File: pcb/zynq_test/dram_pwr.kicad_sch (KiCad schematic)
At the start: 47 parts, among them U401 MT41K256M16TW-107, U402 MT41K256M16TW-107, U501 LP2998

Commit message: Finished Power Supply
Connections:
- net +3.3V renamed +3V3
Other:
- title: (none) -> DDR3 Power
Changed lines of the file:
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@@
 	(paper "A4")
 	(title_block
-		(date "2025-09-06")
-		(rev "v1.0")
+		(title "DDR3 Power")
+		(date "2025-09-13")
+		(rev "A")
 	)
 	(rectangle
@@
 			)
 		)
-		(property "Value" "+3.3V"
+		(property "Value" "+3V3"
 			(at 203.2 80.01 0)
 			(effects

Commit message: Finished to first ddr ic
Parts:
- U401, U402: footprint dram:BGA96C80P9X16_1400X800X120 -> dram:BGA96C80P9X16_1400X800X120_pinDelays
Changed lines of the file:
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@@
 			)
 		)
-		(property "Footprint" "dram:BGA96C80P9X16_1400X800X120"
+		(property "Footprint" "dram:BGA96C80P9X16_1400X800X120_pinDelays"
 			(at 111.76 83.82 0)
 			(effects
@@
 			)
 		)
-		(property "Footprint" "dram:BGA96C80P9X16_1400X800X120"
+		(property "Footprint" "dram:BGA96C80P9X16_1400X800X120_pinDelays"
 			(at 113.03 163.83 0)
 			(effects

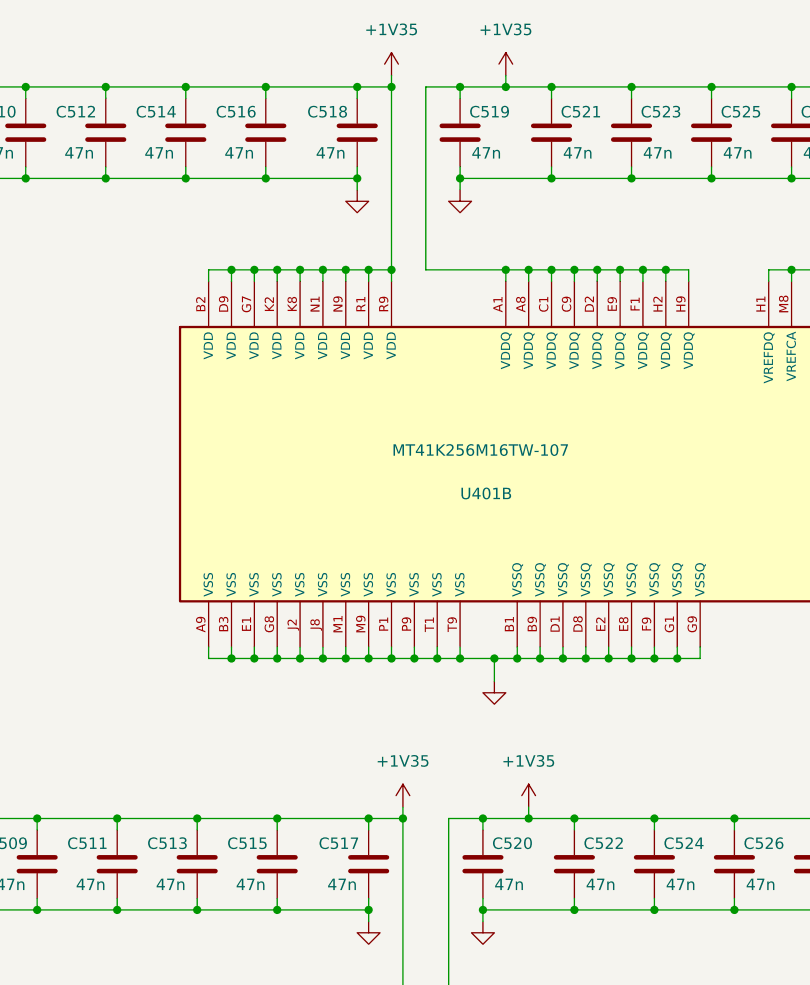
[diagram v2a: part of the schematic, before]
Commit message: DDR routed
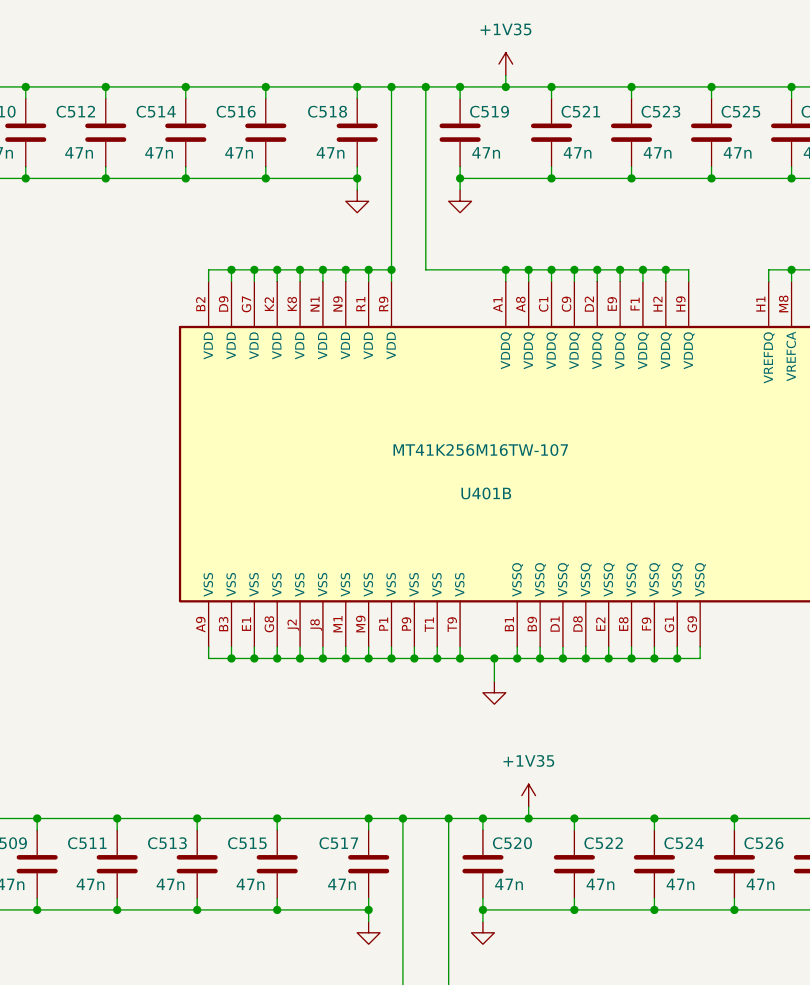
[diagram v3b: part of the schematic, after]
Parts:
- C501, C502, C503, C504, C505, C506, C507, C508, C509, C510, C511, C512, C513, C514, C515, C516, C517, C518, C519, C520, C521, C522, C523, C524, C525, C526, C527, C528, C529, C530, C531, C532, C533, C534, C535, C536, C537, C538, C539, C540: footprint (none) -> Capacitor_SMD:C_0402_1005Metric

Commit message: finished diff of HDMI
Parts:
- C542, C543: footprint (none) -> Capacitor_SMD:C_1210_3225Metric
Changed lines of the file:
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@@
 			)
 		)
-		(property "Footprint" ""
+		(property "Footprint" "Capacitor_SMD:C_1210_3225Metric"
 			(at 254 99.06 0)
 			(effects
@@
 			)
 		)
-		(property "Footprint" ""
+		(property "Footprint" "Capacitor_SMD:C_1210_3225Metric"
 			(at 243.84 99.06 0)
 			(effects

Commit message: Almost done with BOM
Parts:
- added C545: 100n, Capacitor_SMD:C_0402_1005Metric, symbol Device:C_Small
- C540: renamed from C541; footprint (none) -> Capacitor_SMD:C_1210_3225Metric
- C544: footprint (none) -> Capacitor_SMD:C_0402_1005Metric
- U501: footprint (none) -> Package_SO:TI_SO-PowerPAD-8_ThermalVias
- renumbered C502 to C501, C501 to C502, C504 to C503, C503 to C504, C506 to C505, C505 to C506, C508 to C507, C507 to C508, C510 to C509, C509 to C510, C512 to C511, C511 to C512, C514 to C513, C513 to C514, C516 to C515, C515 to C516, C518 to C517, C517 to C518, C530 to C529, C531 to C530, C529 to C531, C540 to C541
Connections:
- net +1V35: now also C545.1
- net GND: now also U501.9 (GND), C545.2

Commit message: Version sent to JLCPCB
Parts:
- C501, C502, C537, C538: JLCPCB Part# (none) -> C88946; PART_NUMBER (none) -> GRM155R71A474KE01D
- C503, C504, C505, C506, C507, C508, C509, C510, C511, C512, C513, C514, C515, C516, C517, C518, C519, C520, C521, C522, C523, C524, C525, C526, C527, C528, C529, C532, C533, C534, C535, C536: JLCPCB Part# (none) -> C77017; PART_NUMBER (none) -> GRM155R71E473KA88D
- C530, C531: JLCPCB Part# (none) -> C77013; PART_NUMBER (none) -> GRM155R71E103KA01D
- C539, C541: JLCPCB Part# (none) -> C23733; PART_NUMBER (none) -> CL05A475MP5NRNC
- C540: JLCPCB Part# (none) -> C525654; PART_NUMBER (none) -> CL32A476KPJNNNE
- C542, C543: JLCPCB Part# (none) -> C23742; PART_NUMBER (none) -> CL32A107MPVNNNE
- C544, C545: JLCPCB Part# (none) -> C1525; PART_NUMBER (none) -> CL05B104KO5NNNC
- U401, U402: JLCPCB Part# (none) -> C367428; PART_NUMBER (none) -> MT41K256M16TW-107 IT:P
- U501: JLCPCB Part# (none) -> C181400; PART_NUMBER (none) -> LP2998MRX/NOPB
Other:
- moved on the sheet: C540, C545
